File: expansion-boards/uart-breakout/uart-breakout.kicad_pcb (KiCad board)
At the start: 4 copper layers, 150 x 90 mm, 54 parts, among them J1 Conn_01x03, J10 Conn_01x06, J11 Conn_01x06, J12 Conn_01x06, J13 Conn_01x06, J2 Conn_01x06, J3 Conn_01x06, J4 Conn_02x12_Odd_Even, J5 Conn_01x06, J6 Conn_01x06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

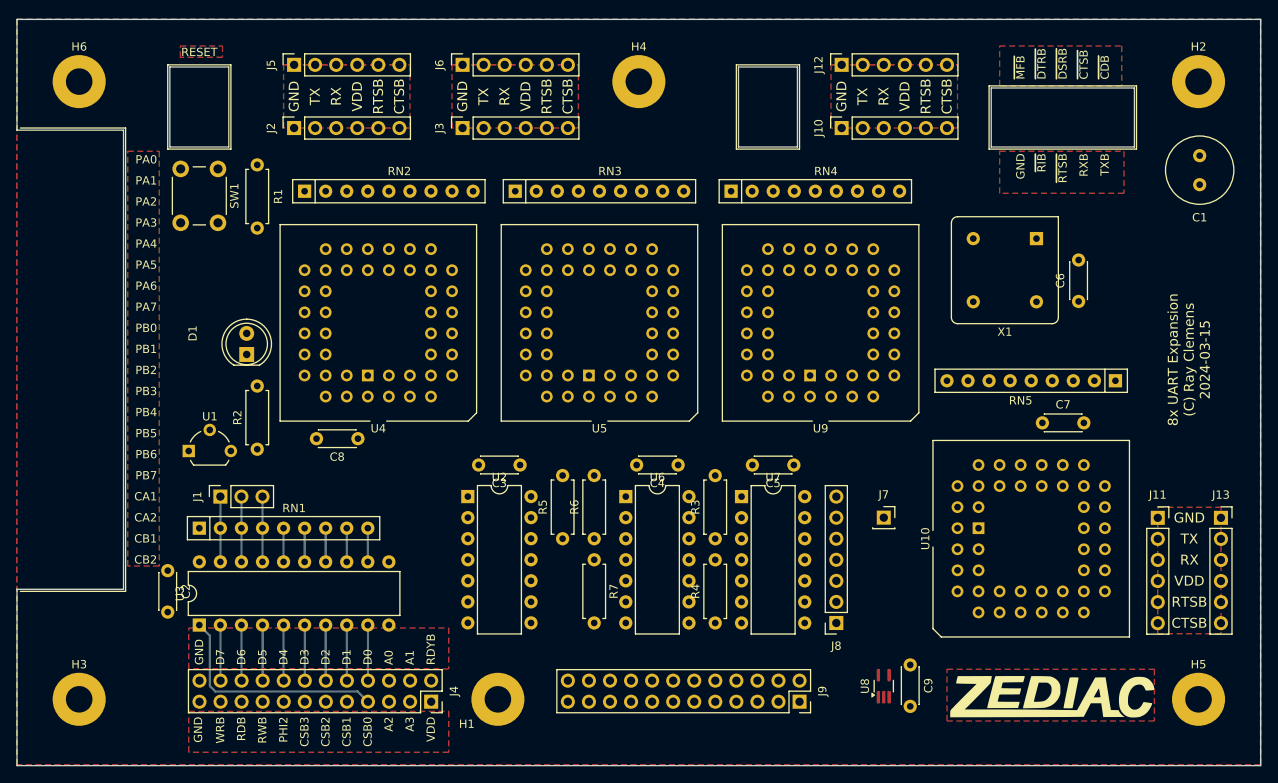
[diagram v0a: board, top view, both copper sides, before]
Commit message: [exp-uart] 90% routed
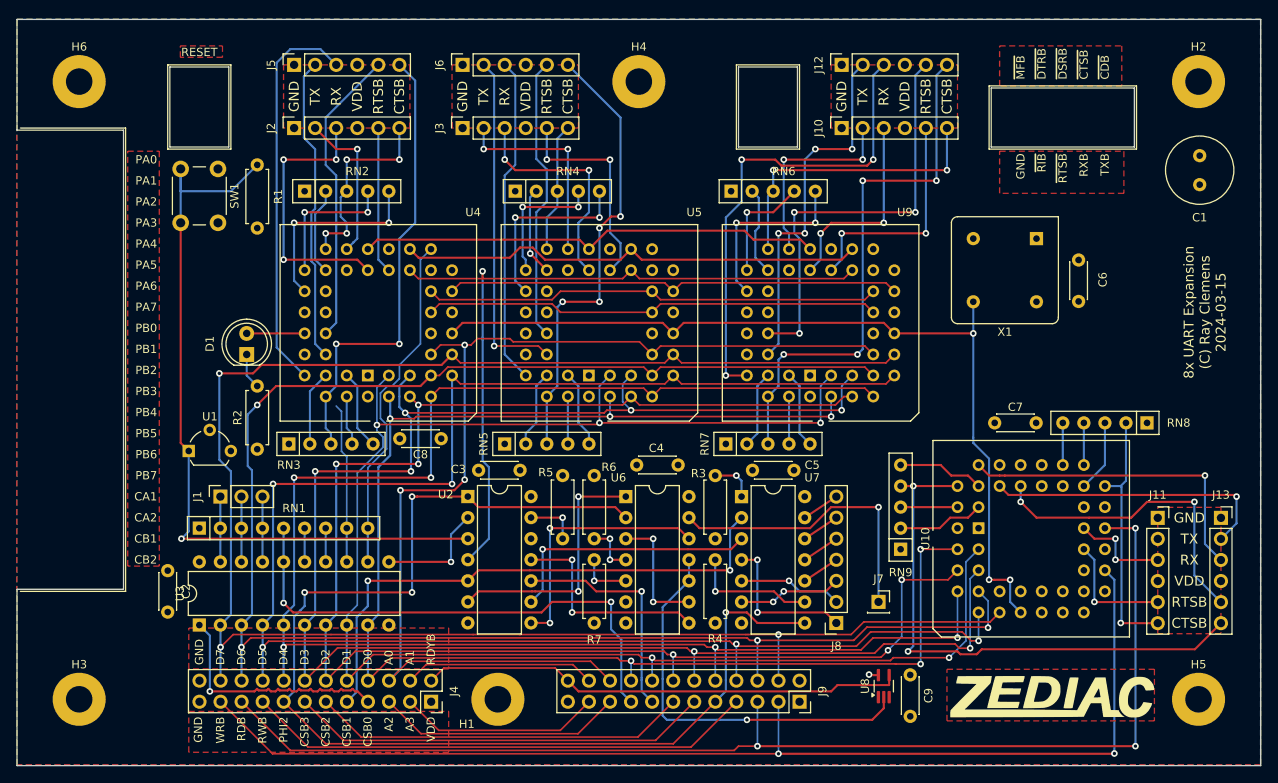
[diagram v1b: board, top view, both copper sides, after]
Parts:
- added RN6: R_Network04, Resistor_THT:R_Array_SIP5, F.Cu at (111.1, 45.7)
- added RN7: R_Network04, Resistor_THT:R_Array_SIP5, F.Cu at (110.5, 76.2)
- added RN8: R_Network04, Resistor_THT:R_Array_SIP5, F.Cu at (161.3, 73.7)
- added RN9: R_Network04, Resistor_THT:R_Array_SIP5, F.Cu at (131.6, 88.9)
- RN2, RN3, RN4, RN5: value 10k -> R_Network04; footprint Resistor_THT:R_Array_SIP9 -> Resistor_THT:R_Array_SIP5
- moved RN5 74.1 mm to (83.8, 76.2), turned to 0 degrees
- moved RN3 40.9 mm to (57.8, 76.2)
- moved RN4 26.0 mm to (85.1, 45.7)
- moved J7 10.2 mm to (128.9, 95.2)
- moved C8 5.04 mm to (71.2, 75.6), turned to 0 degrees
- moved C9 1.20 mm to (132.7, 104.1)
- moved C7 0.75 mm to (147.9, 73.7), turned to 180 degrees
- moved C3 0.64 mm to (85.7, 79.4)
- moved C5 0.63 mm to (118.7, 79.4)
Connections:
- J9 pad 1: VDD -> GND
- J9 pad 10: /D1 -> /D4
- J9 pad 11: /AUXCSB2 -> /AUXCSB3
- J9 pad 12: /D2 -> /D3
- J9 pad 13: /AUXCSB3 -> /AUXCSB2
- J9 pad 14: /D3 -> /D2
- J9 pad 15: /PHI2 -> /CSB_SLOW
- J9 pad 16: /D4 -> /D1
- J9 pad 17: /RWB -> /B4
- J9 pad 18: /D5 -> /D0
- J9 pad 19: /RDB -> /A2
- J9 pad 2: //RDY -> GND
- J9 pad 20: /D6 -> /A0
- J9 pad 21: /WRB -> /A3
- J9 pad 22: /D7 -> /A1
- J9 pad 23: GND -> VDD
- J9 pad 24: GND -> //RDY
- J9 pad 3: /A3 -> /WRB
- J9 pad 4: /A1 -> /D7
- J9 pad 5: /A2 -> /RDB
- J9 pad 6: /A0 -> /D6
- J9 pad 7: /B4 -> /RWB
- J9 pad 8: /D0 -> /D5
- J9 pad 9: /CSB_SLOW -> /PHI2
- RN3 pad 2: /~{CD3B} -> /~{DSR0B}
- RN3 pad 3: /~{CTS3B} -> /~{CTS0B}
- RN3 pad 4: /~{DSR3B} -> /~{CD0B}
- RN3 pad 5: /~{RI3B} -> /~{RI0B}
- RN4 pad 2: /~{CD5B} -> /~{CD3B}
- RN4 pad 3: /~{CTS5B} -> /~{CTS3B}
- RN4 pad 4: /~{DSR5B} -> /~{DSR3B}
- RN4 pad 5: /~{RI5B} -> /~{RI3B}
- RN5 pad 2: /~{CD7B} -> /~{DSR2B}
- RN5 pad 3: /~{CTS7B} -> /~{CTS2B}
- RN5 pad 4: /~{DSR7B} -> /~{CD2B}
- RN5 pad 5: /~{RI7B} -> /~{RI2B}
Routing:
- net /D7: track 6.71 -> 223.5 mm, vias 0 -> 3
- net /D6: track 6.71 -> 212.9 mm, vias 0 -> 4
- net /D5: track 6.71 -> 209.8 mm, vias 0 -> 5
- net /D3: track 6.71 -> 208.7 mm, vias 0 -> 7
- net /RDB: track 0.00 -> 201.9 mm, vias 0 -> 3
- net /WRB: track 0.00 -> 195.7 mm, vias 0 -> 2
- net /D4: track 6.71 -> 198.2 mm, vias 0 -> 5
- net /D1: track 6.71 -> 197.3 mm, vias 0 -> 5
- net /D2: track 6.71 -> 188.1 mm, vias 0 -> 6
- net /D0: track 6.71 -> 182.3 mm, vias 0 -> 6
- net /PHI2: track 0.00 -> 143.2 mm, vias 0 -> 4
- net /A0: track 0.00 -> 132.4 mm, vias 0 -> 3
- net Net-(U10-XTAL1): track 0.00 -> 106.3 mm, vias 0 -> 3
- net Net-(U1-RST): track 0.00 -> 93.2 mm, vias 0 -> 1
- net /RES: track 0.00 -> 92.1 mm, vias 0 -> 1
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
